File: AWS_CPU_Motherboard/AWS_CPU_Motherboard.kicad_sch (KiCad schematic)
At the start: 52 parts, among them J1 Power, J10 UART B, J12 Video, J14 HDD Power, J15 HDD Power, J2 Speaker, J3 Cluster, J4 Cluster, J5 HDD Power, J6 Drive Type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

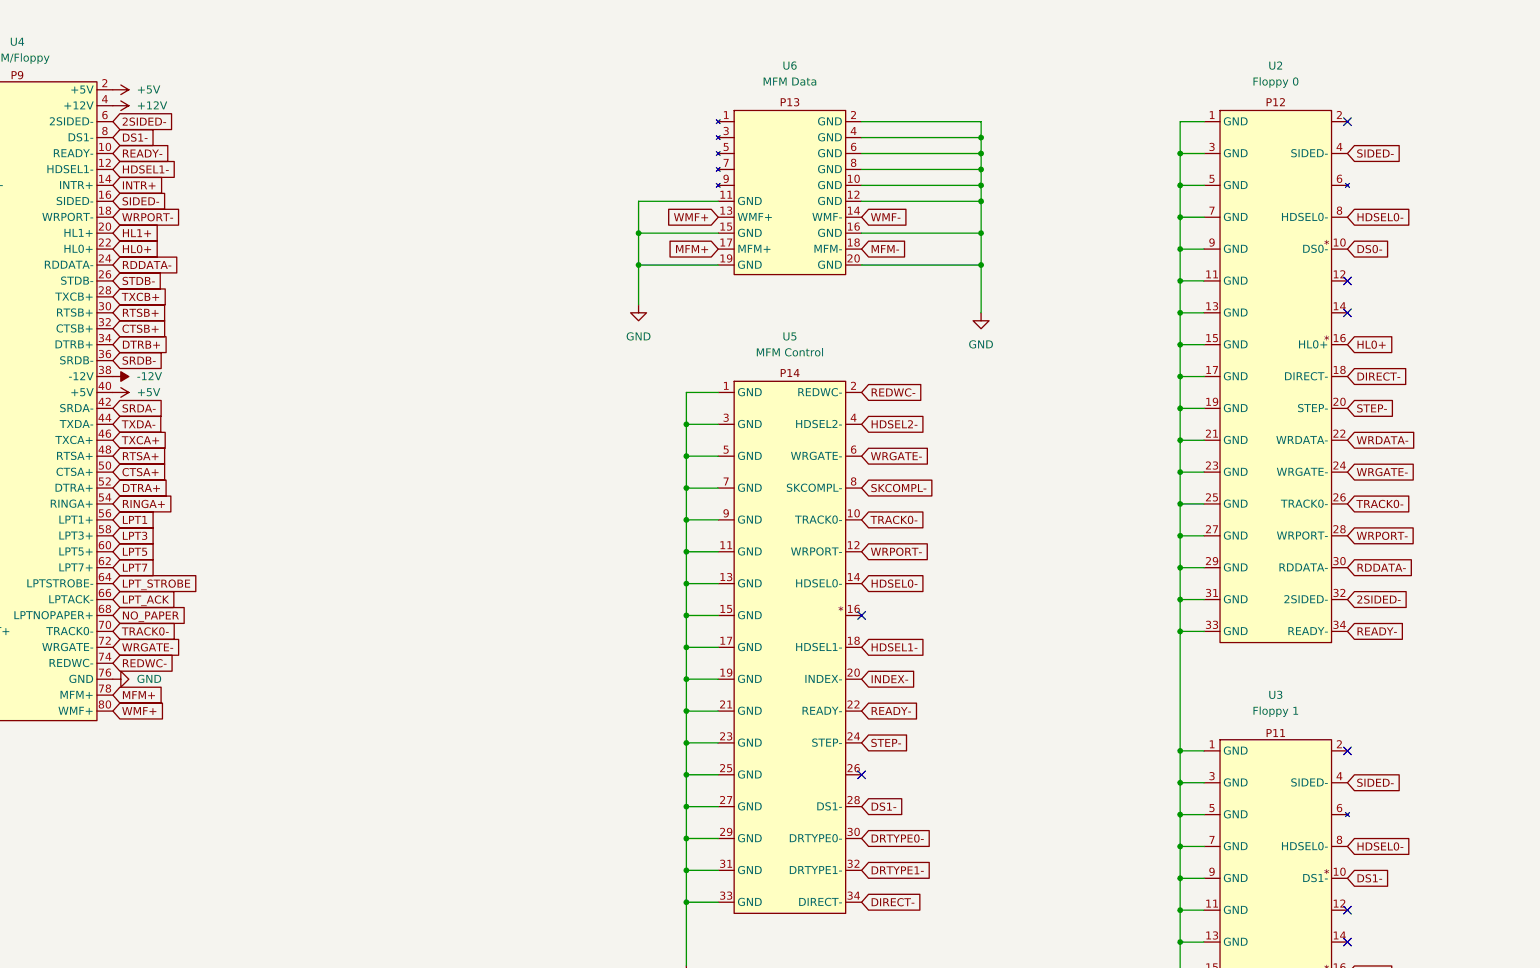
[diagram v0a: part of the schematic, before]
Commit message: Update PCB to fix floppy drive & update video software to capure all the screen
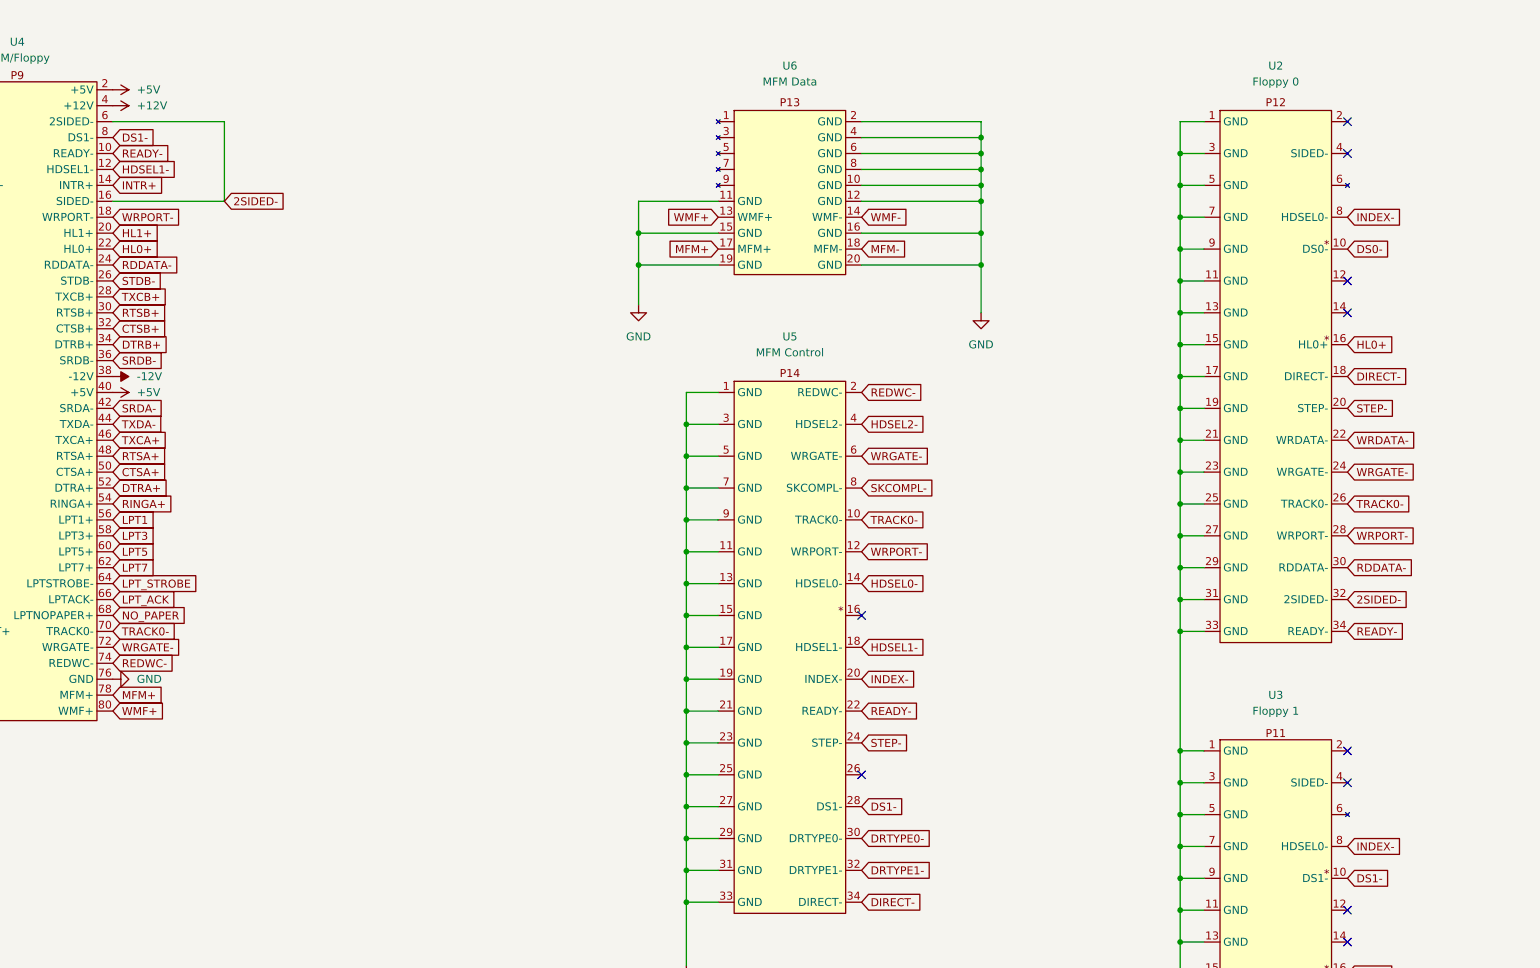
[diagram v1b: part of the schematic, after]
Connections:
- net 2SIDED-: now also U4.16 (SIDED-)
- net HDSEL0-: no longer U2.8 (HDSEL0-), U3.8 (HDSEL0-)
- net INDEX-: now also U2.8 (HDSEL0-), U3.8 (HDSEL0-)
- removed net SIDED-: U2.4 (SIDED-), U3.4 (SIDED-), U4.16 (SIDED-)
- no-connect marks 39 -> 41
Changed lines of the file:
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@@
 	)
 	(no_connect
+		(at 528.32 41.91)
+	)
+	(no_connect
 		(at 118.11 298.45)
 	)
@@
 	)
 	(no_connect
+		(at 528.32 142.24)
+	)
+	(no_connect
 		(at 125.73 326.39)
 	)
@@
 	(wire
 		(pts
+			(xy 331.47 49.53) (xy 349.25 49.53)
+		)
+		(stroke
+			(width 0)
+			(type default)
+		)
+	)
+	(wire
+		(pts
 			(xy 422.91 120.65) (xy 427.99 120.65)
 		)
@@
 	(wire
 		(pts
+			(xy 349.25 36.83) (xy 349.25 49.53)
+		)
+		(stroke
+			(width 0)
+			(type default)
+		)
+	)
+	(wire
+		(pts
 			(xy 501.65 46.99) (xy 505.46 46.99)
 		)
@@
 	(wire
 		(pts
+			(xy 331.47 36.83) (xy 349.25 36.83)
+		)
+		(stroke
+			(width 0)
+			(type default)
+		)
+	)
+	(wire
+		(pts
 			(xy 78.74 340.36) (xy 99.06 340.36)
 		)
@@
 		)
 	)
+	(global_label "2SIDED-"
+		(shape input)
+		(at 349.25 49.53 0)
+		(fields_autoplaced yes)
+		(effects
+			(font
+				(size 1.27 1.27)
+			)
+			(justify left)
+		)
+		(property "Intersheetrefs" "${INTERSHEET_REFS}"
+			(at 360.5204 49.53 0)
+			(effects
+				(font
+					(size 1.27 1.27)
+				)
+				(justify left)
+				(hide yes)
+			)
+		)
+	)
 	(global_label "VIDEO+"
 		(shape output)
@@
 		)
 	)
-	(global_label "2SIDED-"
-		(shape input)
-		(at 331.47 36.83 0)
-		(fields_autoplaced yes)
-		(effects
-			(font
-				(size 1.27 1.27)
-			)
-			(justify left)
-		)
-		(property "Intersheetrefs" "${INTERSHEET_REFS}"
-			(at 342.7404 36.83 0)
-			(effects
-				(font
-					(size 1.27 1.27)
-				)
-				(justify left)
-				(hide yes)
-			)
-		)
-	)
-	(global_label "HDSEL0-"
-		(shape input)
-		(at 528.32 152.4 0)
-		(fields_autoplaced yes)
-		(effects
-			(font
-				(size 1.27 1.27)
-			)
-			(justify left)
-		)
-		(property "Intersheetrefs" "${INTERSHEET_REFS}"
-			(at 540.0742 152.4 0)
-			(effects
-				(font
-					(size 1.27 1.27)
-				)
-				(justify left)
-				(hide yes)
-			)
-		)
-	)
 	(global_label "DS0-"
 		(shape input)
@@
 		)
 	)
+	(global_label "INDEX-"
+		(shape input)
+		(at 528.32 152.4 0)
+		(fields_autoplaced yes)
+		(effects
+			(font
+				(size 1.27 1.27)
+			)
+			(justify left)
+		)
+		(property "Intersheetrefs" "${INTERSHEET_REFS}"
+			(at 538.4414 152.4 0)
+			(effects
+				(font
+					(size 1.27 1.27)
+				)
+				(justify left)
+				(hide yes)
+			)
+		)
+	)
 	(global_label "LPT_SELECT"
 		(shape input)
@@
 		)
 	)
-	(global_label "HDSEL0-"
-		(shape input)
-		(at 528.32 52.07 0)
-		(fields_autoplaced yes)
-		(effects
-			(font
-				(size 1.27 1.27)
-			)
-			(justify left)
-		)
-		(property "Intersheetrefs" "${INTERSHEET_REFS}"
-			(at 540.0742 52.07 0)
-			(effects
-				(font
-					(size 1.27 1.27)
-				)
-				(justify left)
-				(hide yes)
-			)
-		)
-	)
 	(global_label "LPT2"
 		(shape input)
@@
 		)
 	)
+	(global_label "INDEX-"
+		(shape input)
+		(at 528.32 52.07 0)
+		(fields_autoplaced yes)
+		(effects
+			(font
+				(size 1.27 1.27)
+			)
+			(justify left)
+		)
+		(property "Intersheetrefs" "${INTERSHEET_REFS}"
+			(at 538.4414 52.07 0)
+			(effects
+				(font
+					(size 1.27 1.27)
+				)
+				(justify left)
+				(hide yes)
+			)
+		)
+	)
 	(global_label "HORDR+"
 		(shape output)
@@
 		)
 	)
-	(global_label "SIDED-"
-		(shape input)
-		(at 528.32 41.91 0)
-		(fields_autoplaced yes)
-		(effects
-			(font
-				(size 1.27 1.27)
-			)
-			(justify left)
-		)
-		(property "Intersheetrefs" "${INTERSHEET_REFS}"
-			(at 538.3809 41.91 0)
-			(effects
-				(font
-					(size 1.27 1.27)
-				)
-				(justify left)
-				(hide yes)
-			)
-		)
-	)
 	(global_label "VIDEO-"
 		(shape output)
@@
 		)
 	)
-	(global_label "SIDED-"
-		(shape input)
-		(at 528.32 142.24 0)
-		(fields_autoplaced yes)
-		(effects
-			(font
-				(size 1.27 1.27)
-			)
-			(justify left)
-		)
-		(property "Intersheetrefs" "${INTERSHEET_REFS}"
-			(at 538.3809 142.24 0)
-			(effects
-				(font
-					(size 1.27 1.27)
-				)
-				(justify left)
-				(hide yes)
-			)
-		)
-	)
 	(global_label "CPU_RXCA-"
 		(shape passive)
@@
 			(effects
 				(font
-					(size 1.27 1.27)
-				)
-				(justify left)
-				(hide yes)
-			)
-		)
-	)
-	(global_label "SIDED-"
-		(shape input)
-		(at 331.47 49.53 0)
-		(fields_autoplaced yes)
-		(effects
-			(font
-				(size 1.27 1.27)
-			)
-			(justify left)
-		)
-		(property "Intersheetrefs" "${INTERSHEET_REFS}"
-			(at 341.5309 49.53 0)
-			(effects
-				(font
